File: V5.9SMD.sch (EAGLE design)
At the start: 37 parts, among them IC1 TL084D

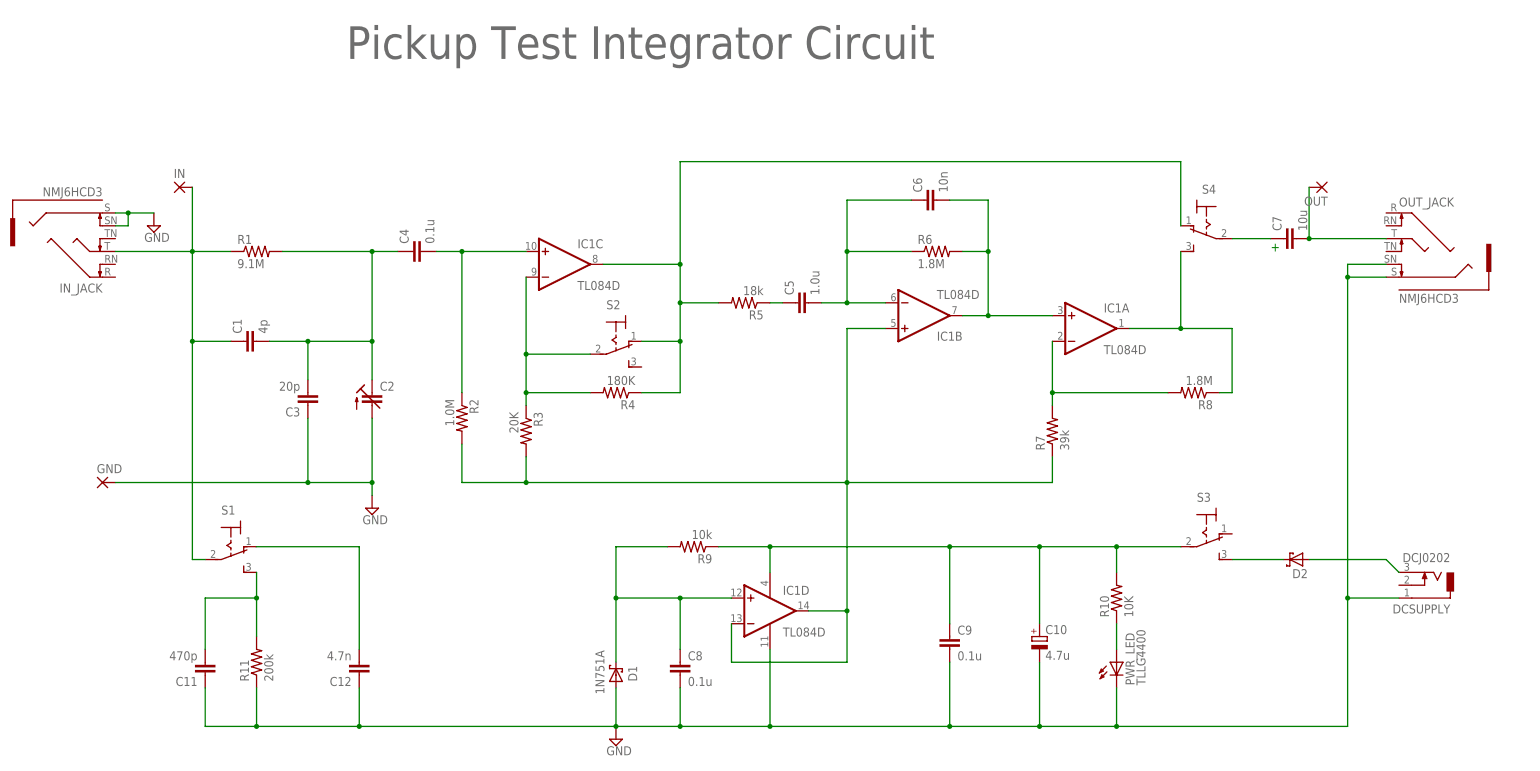
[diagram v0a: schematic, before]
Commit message: Updated bypass and i/o jacks
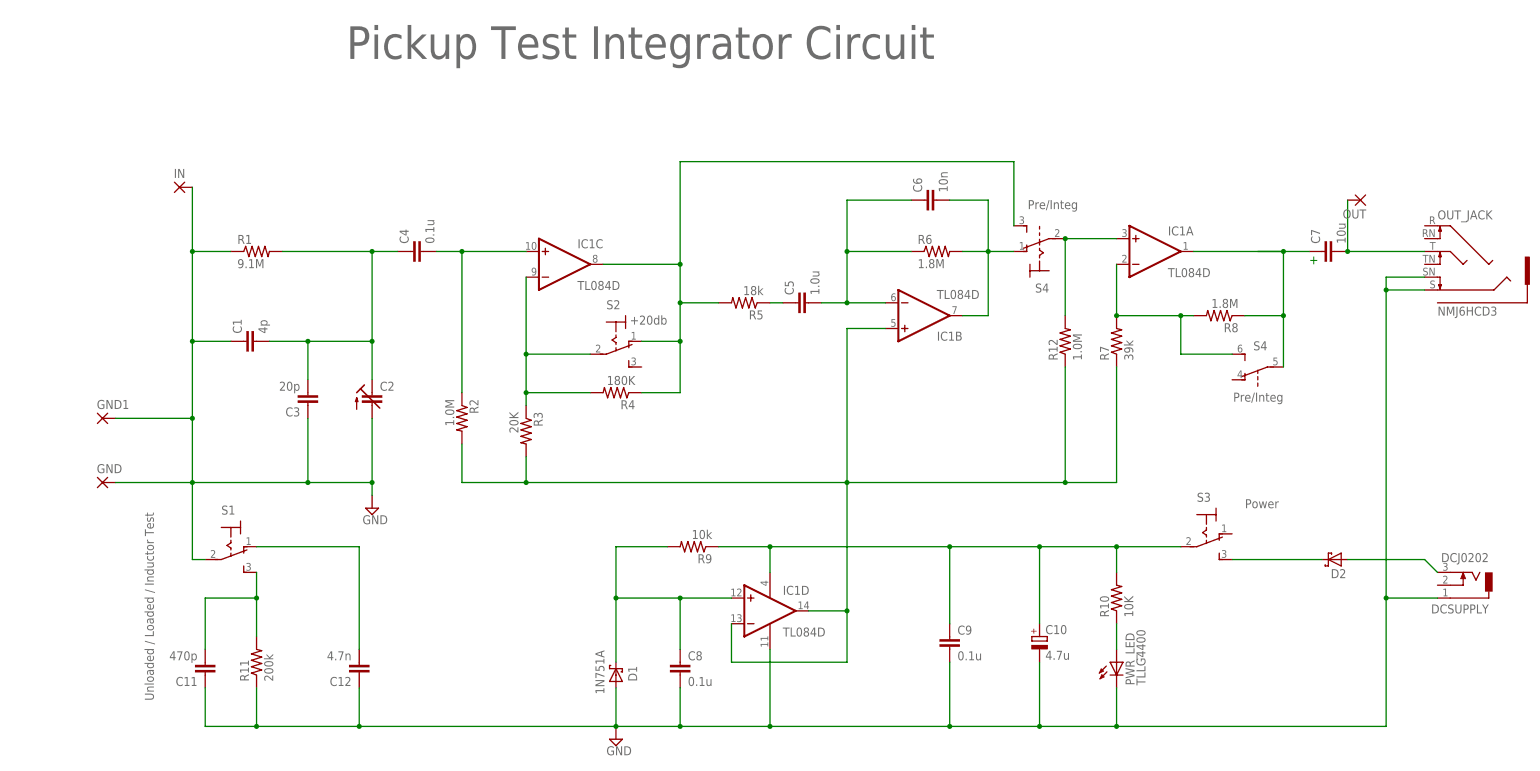
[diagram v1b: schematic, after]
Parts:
- removed IN_JACK: NMJ6HCD3, Heliostat:NMJ6HCD3
- added GND1: (no value), wirepad:2,54/1,1
- added R12: 1.0M, rcl:R-US_R0805
- S4: device switch:320-916 -> switch:320-938
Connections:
- removed net N$13: C1.1, IN.P, IN_JACK.T, R1.1, S1.P
- removed net N$17: C7.1, S4.P
- new net N$11: IC1A.+IN, R12.2, S41.P
- net GND: now also C1.1, GND1.P, IN.P, R1.1, S1.P; no longer IN_JACK.S, IN_JACK.SN
- net N$14: now also R12.1
- net N$4: now also S41.S; no longer S4.O
- net N$6: now also S41.O; no longer IC1A.+IN
- net N$7: now also S4B.S
- net N$8: now also C7.1, S4B.P; no longer S4.S
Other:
- note added: "+20db"
- note added: "Power"
- note added: "Pre/Integ"
- note added: "Unloaded / Loaded / Inductor Test"
- moved on the sheet: C7, D2, DCSUPPLY, IC1A, OUT, OUT_JACK, R7, R8
